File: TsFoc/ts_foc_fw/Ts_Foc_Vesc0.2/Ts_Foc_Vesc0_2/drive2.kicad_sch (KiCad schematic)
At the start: 31 parts, among them Q10 RU3089M-C, Q11 RU3089M-C, Q12 RU3089M-C, Q13 RU3089M-C, Q8 RU3089M-C, Q9 RU3089M-C, U7 EG2133, U8 INA240A2PWR, U9 INA240A2PWR

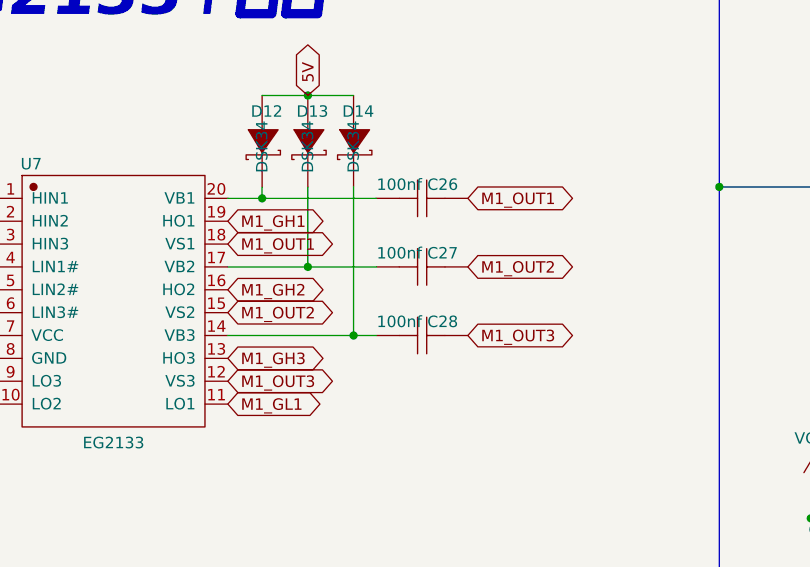
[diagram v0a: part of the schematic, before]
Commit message: 1. can通信测试通过 2. as5600通信测试通过 3. PCB板桥驱动电路有标签错误，导致有四个引脚未能链接 4.
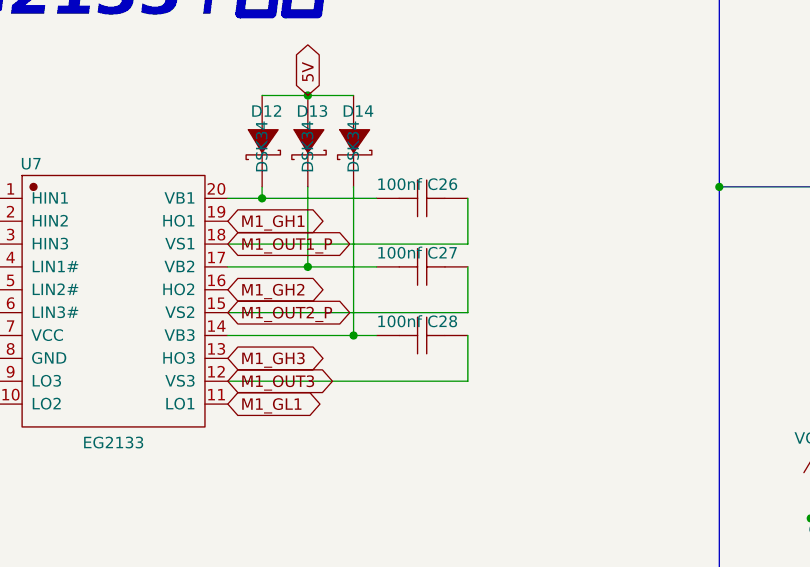
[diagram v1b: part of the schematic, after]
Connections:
- net M1_OUT1 is gone; now on net M1_OUT1_P: C26.1, U7.18 (VS1)
- net M1_OUT2 is gone; now on net M1_OUT2_P: C27.1, U7.15 (VS2)
